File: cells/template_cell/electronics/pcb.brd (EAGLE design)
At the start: 49.6 x 49.9 mm, 28 parts, among them M1 M02PTH3, M2 M02PTH3, Q1 MOSFET-NCHANNEL2N7000, Q2 MOSFET-NCHANNEL2N7000, SW0 M01PTH_LONGPAD, SW1 M02PTH3, SW2 M02PTH3, SW3 M02PTH3, SW4 M02PTH3, SW5 M02PTH3

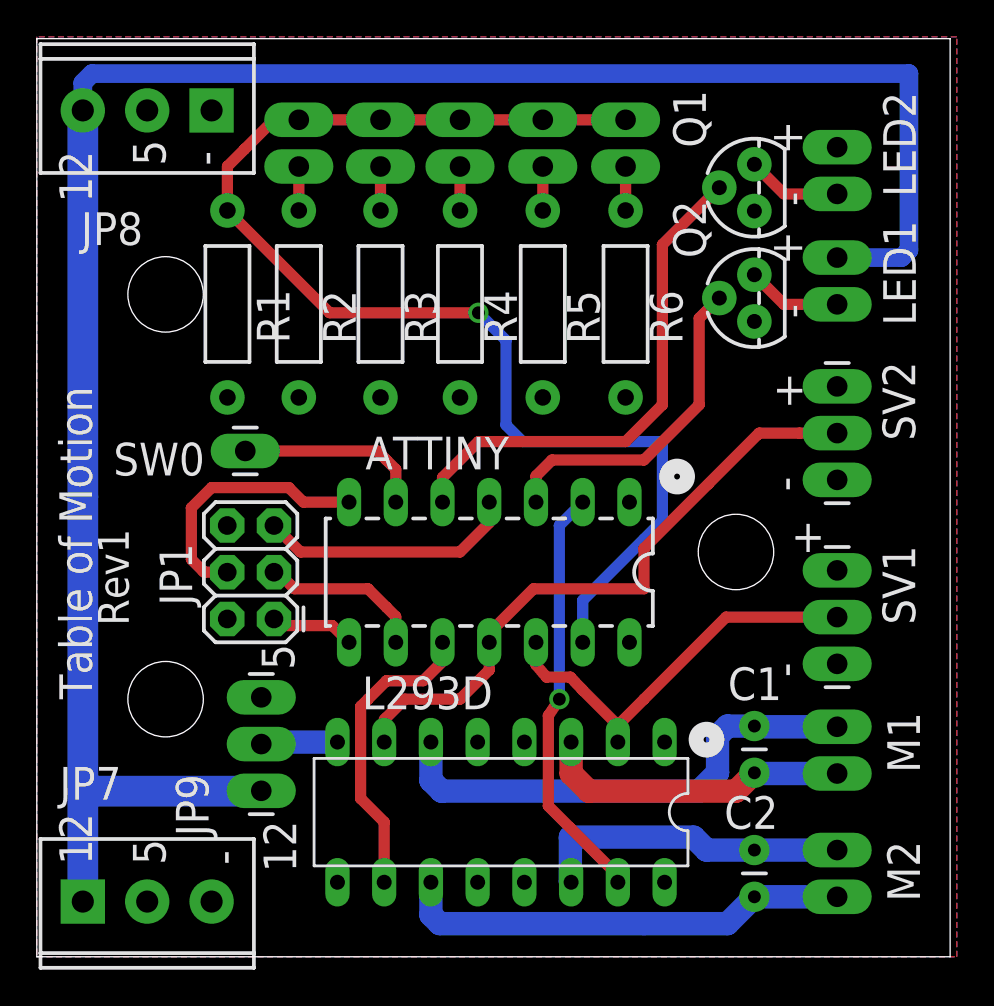
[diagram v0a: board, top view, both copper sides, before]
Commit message: Moving electronics folder to template_cell
template_cell folder should contain all the things necessary to make a
cell, including the generic things like the electronics and basic
reusable parts.
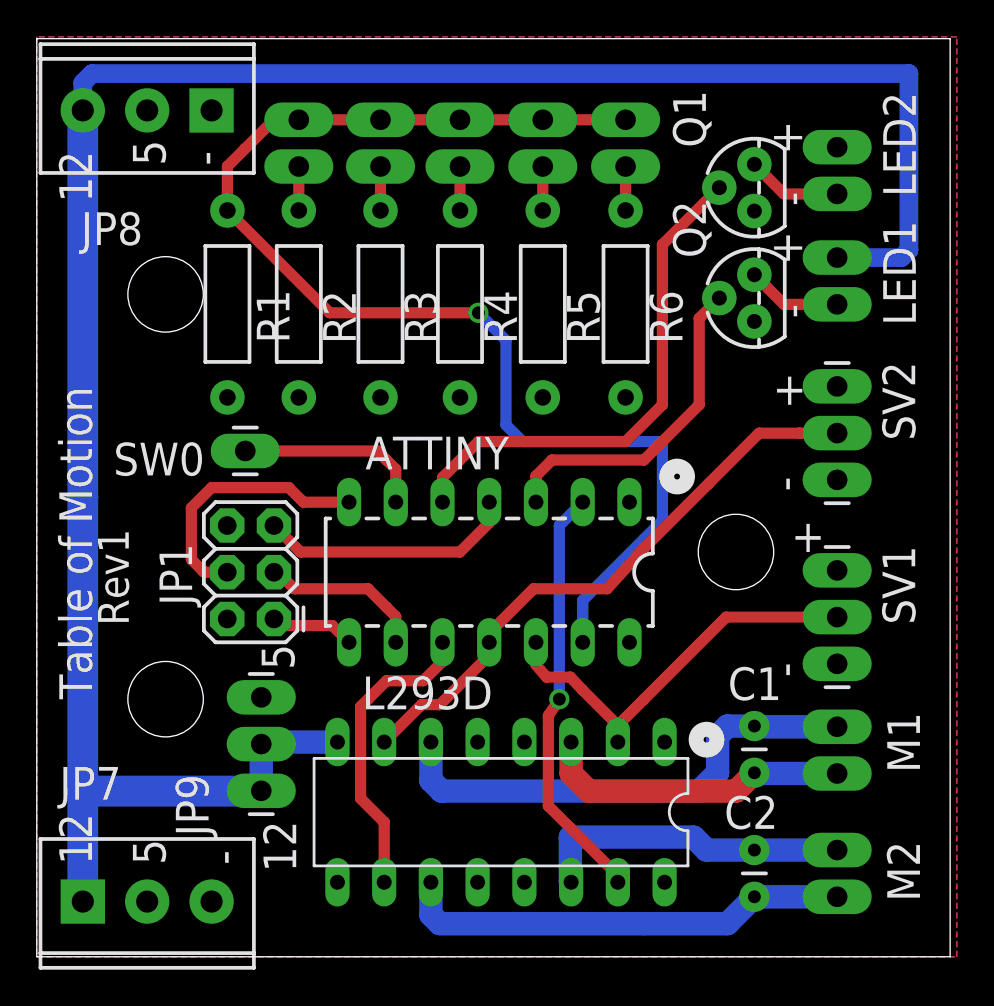
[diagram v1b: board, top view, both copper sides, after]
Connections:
- net N$10 renamed LIMITSWITCH
- net N$11 renamed CONTROL1
- net N$14 renamed MOSI
- net N$15 renamed !RESET
- net N$16 renamed MISO
- net N$2 renamed CONTROL2
- net N$20 renamed LEDCONTROL1
- net N$21 renamed LEDCONTROL2
- net N$4 renamed CONTROL3
- net N$8 renamed SCL
- net N$9 renamed CONTROL4
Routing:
- net N$2: track 0.00 -> 2.50 mm
- net CONTROL2: track 34.7 -> 32.3 mm
